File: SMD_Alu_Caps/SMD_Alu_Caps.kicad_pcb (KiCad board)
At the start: 2 copper layers, 7 parts

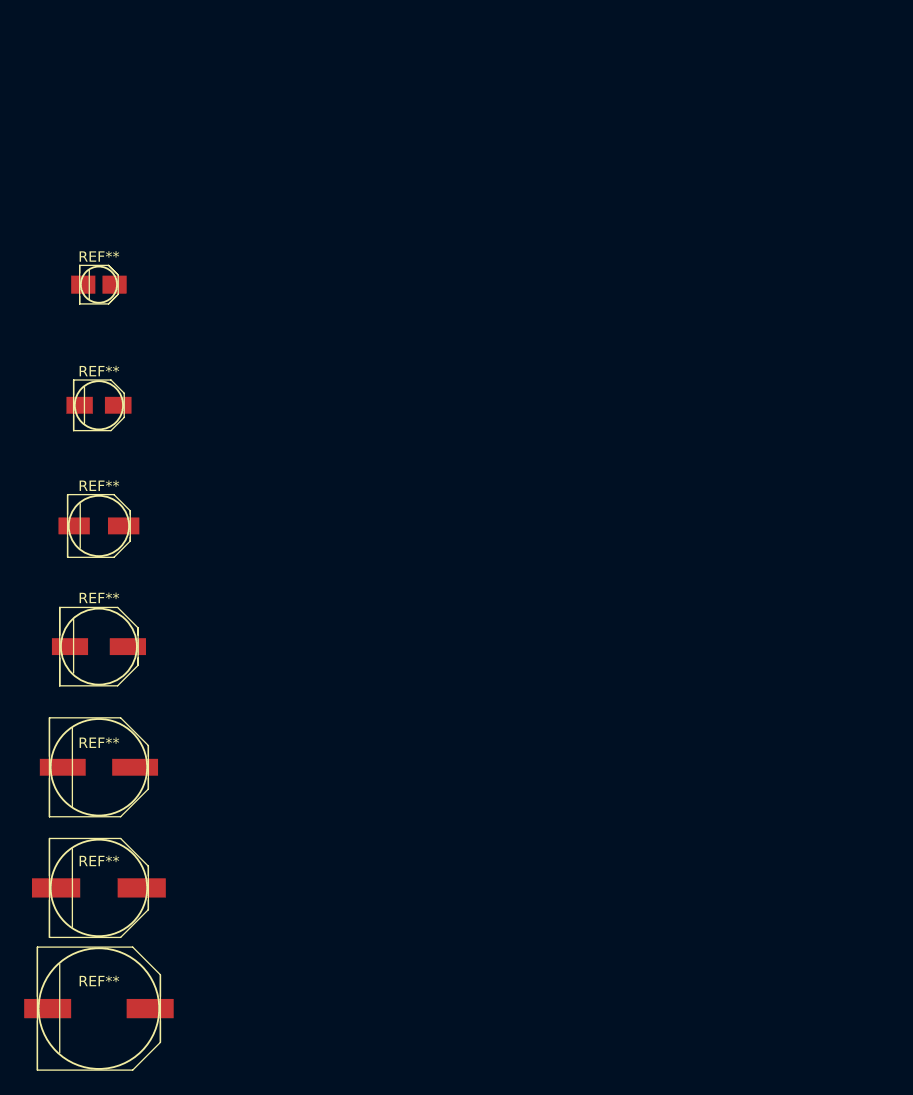
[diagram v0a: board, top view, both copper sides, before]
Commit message: * Renamed directory JST to JST_Conn, as the library is named so.  * Reworked almost from scratch most Panasonic Aluminium Capacitor footprints.  * Added numerous large Panasonic sizes, like G17, H16, J21 etc...
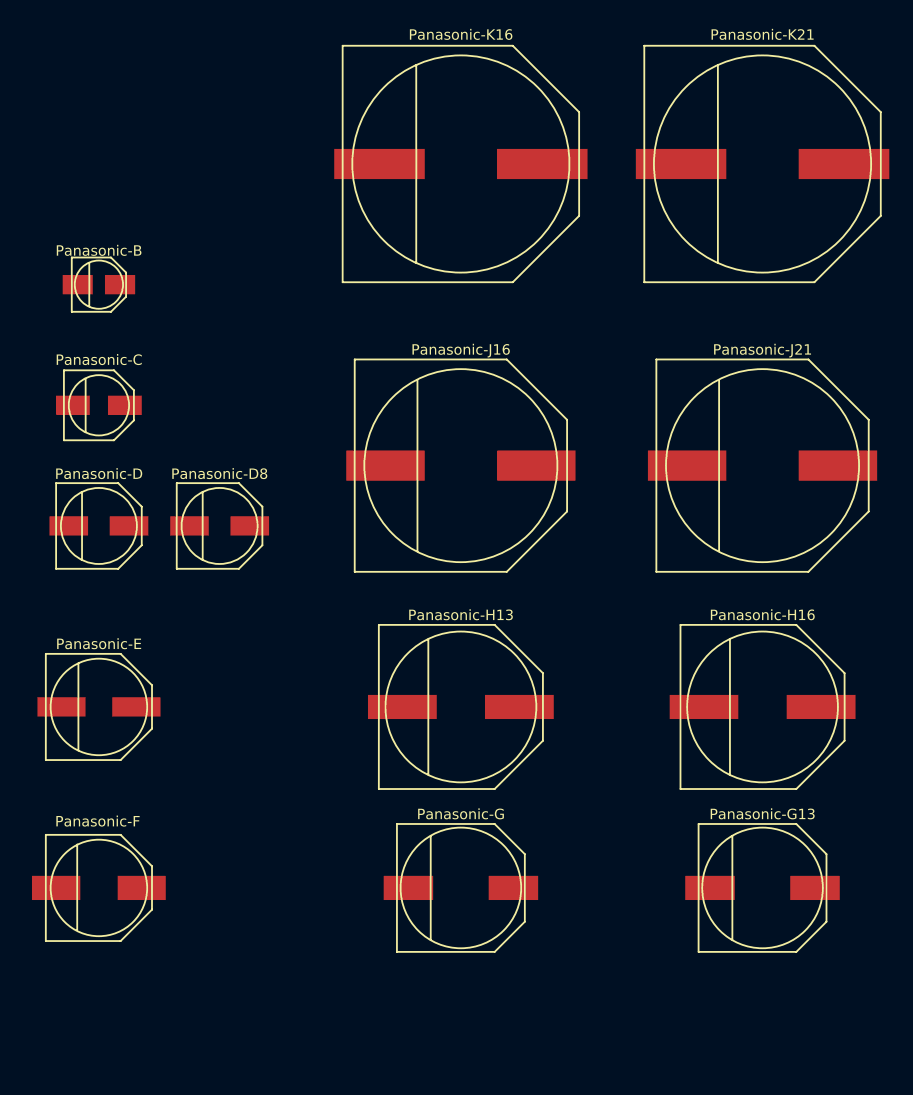
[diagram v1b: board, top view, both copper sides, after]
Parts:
- removed REF**: VAL**, SMD_Alu_Caps:Panasonic-A
- removed REF**: VAL**, SMD_Alu_Caps:Panasonic-B
- removed REF**: VAL**, SMD_Alu_Caps:Panasonic-C
- removed REF**: VAL**, SMD_Alu_Caps:Panasonic-D
- removed REF**: VAL**, SMD_Alu_Caps:Panasonic-E
- removed REF**: VAL**, SMD_Alu_Caps:Panasonic-F
- removed REF**: VAL**, SMD_Alu_Caps:Panasonic-G
- added Panasonic-B: VAL**, SMD_Alu_Caps:Panasonic-B, F.Cu at (100.0, 60.0)
- added Panasonic-C: VAL**, SMD_Alu_Caps:Panasonic-C, F.Cu at (100.0, 70.0)
- added Panasonic-D: VAL**, SMD_Alu_Caps:Panasonic-D, F.Cu at (100.0, 80.0)
- added Panasonic-D8: VAL**, SMD_Alu_Caps:Panasonic-D8, F.Cu at (110.0, 80.0)
- added Panasonic-E: VAL**, SMD_Alu_Caps:Panasonic-E, F.Cu at (100.0, 95.0)
- added Panasonic-F: VAL**, SMD_Alu_Caps:Panasonic-F, F.Cu at (100.0, 110.0)
- added Panasonic-G: VAL**, SMD_Alu_Caps:Panasonic-G, F.Cu at (130.0, 110.0)
- added Panasonic-G13: VAL**, SMD_Alu_Caps:Panasonic-G13, F.Cu at (155.0, 110.0)
- added Panasonic-H13: VAL**, SMD_Alu_Caps:Panasonic-H13, F.Cu at (130.0, 95.0)
- added Panasonic-H16: VAL**, SMD_Alu_Caps:Panasonic-H16, F.Cu at (155.0, 95.0)
- added Panasonic-J16: VAL**, SMD_Alu_Caps:Panasonic-J16, F.Cu at (130.0, 75.0)
- added Panasonic-J21: VAL**, SMD_Alu_Caps:Panasonic-J21, F.Cu at (155.0, 75.0)
- added Panasonic-K16: VAL**, SMD_Alu_Caps:Panasonic-K16, F.Cu at (130.0, 50.0)
- added Panasonic-K21: VAL**, SMD_Alu_Caps:Panasonic-K21, F.Cu at (155.0, 50.0)
